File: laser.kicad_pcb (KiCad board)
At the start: 4 copper layers, 90.2 x 50.9 mm, 129 parts, among them IC201 ADM7172ACPZ-4.2-R7, IC202 LT1716CS5#TRPBF, IC203 ADM7154ARDZ-3.3-R7, IC204 IRF9358PBF, IC601 ATMEGA328P-AU, IC602 FT232RL-TUBE, IC701 MAX6126AASA25+, IC801 ADS122C04IPWR, J601 M20-9980345, J602 USB_Connector, Q401 RSR030N06TL, U101 281698-3, U201 LM4040EIM3X-2.5_NOPB, U301 OPA569AIDWPR, U302 OPA569AIDWPR, U401 ADA4528-2ACPZ-RL, U402 782853152_WE-CBA_08, U501 ADA4528-2ACPZ-RL, U502 ADA4528-2ACPZ-RL, U801 MAX5217GUA+, U802 MAX5217GUA+, Y601 ECS-160-16-33B-CKM-TR

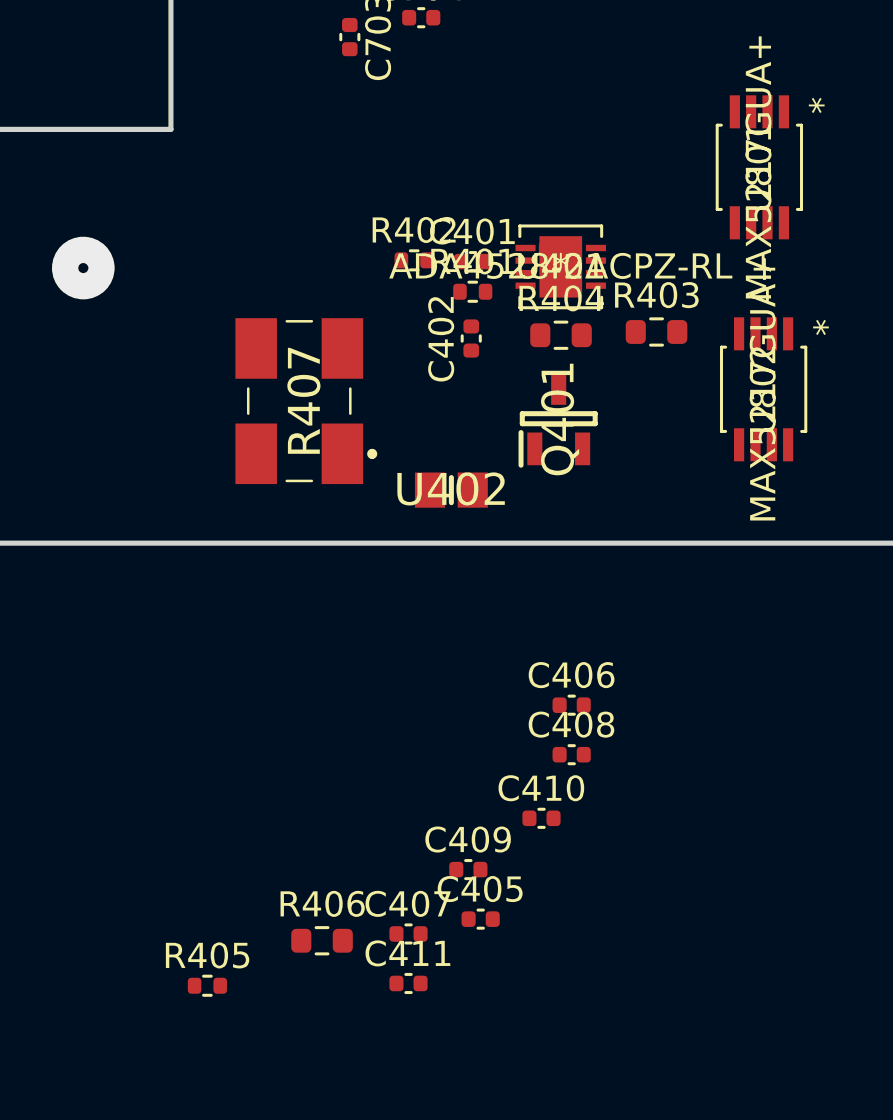
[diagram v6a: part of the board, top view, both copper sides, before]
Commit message: laid out reference and current resistors/caps
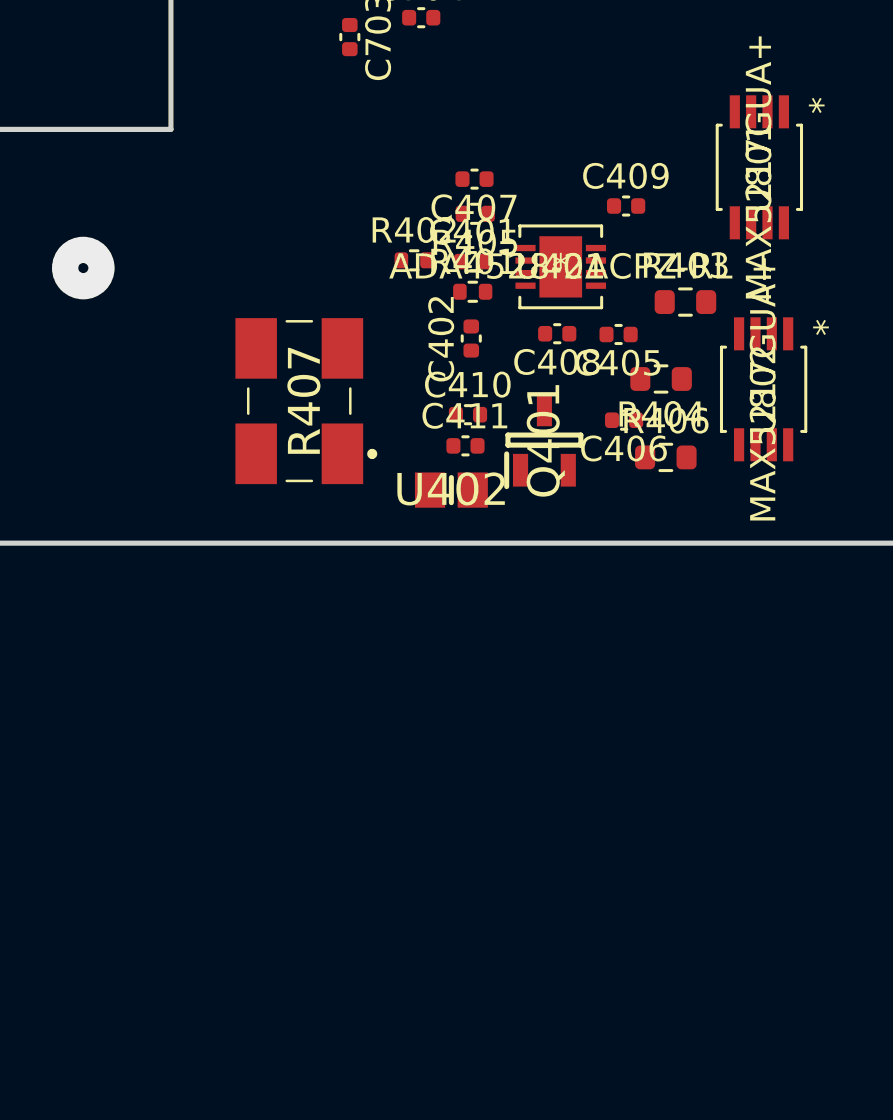
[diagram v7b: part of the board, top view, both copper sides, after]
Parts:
- moved R405 32.5 mm to (167.9, 119.1), turned to 180 degrees
- moved C407 30.1 mm to (167.9, 117.7), turned to 180 degrees
- moved C409 27.1 mm to (173.9, 118.8)
- moved C405 23.9 mm to (173.6, 123.9), turned to 180 degrees
- moved R406 23.6 mm to (175.5, 128.8)
- moved C411 21.5 mm to (167.5, 128.3)
- moved C408 16.8 mm to (171.2, 123.9), turned to 180 degrees
- moved C410 16.3 mm to (167.6, 127.1)
- moved C406 11.5 mm to (173.8, 127.3), turned to 180 degrees
- moved R404 4.34 mm to (175.3, 125.7), turned to 180 degrees
- moved R403 1.65 mm to (176.2, 122.6)
- moved Q401 1.02 mm to (170.6, 128.1)
- moved C403 0.13 mm to (171.3, 120.6)
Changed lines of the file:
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@@
   )
   (module Capacitor_SMD:C_0402_1005Metric (layer B.Cu)
-    (at 171.18 120.52)
+    (at 171.28 120.6)
     (descr "Capacitor SMD 0402 (1005 Metric), square (rectangular) end terminal, IPC_7351 nominal, (Body size source: IPC-SM-782 page 76, https://www.pcb-3d.com/wordpress/wp-content/uploads/ipc-sm-782a_amendment_1_and_2.pdf), generated with kicad-footprint-generator")
     (tags capacitor)
@@
   )
   (module Capacitor_SMD:C_0402_1005Metric (layer F.Cu)
-    (at 168.105001 147.165001)
+    (at 173.59 123.91 180)
     (descr "Capacitor SMD 0402 (1005 Metric), square (rectangular) end terminal, IPC_7351 nominal, (Body size source: IPC-SM-782 page 76, https://www.pcb-3d.com/wordpress/wp-content/uploads/ipc-sm-782a_amendment_1_and_2.pdf), generated with kicad-footprint-generator")
     (tags capacitor)
@@
       (effects (font (size 0.25 0.25) (thickness 0.04)))
     )
-    (pad 2 smd roundrect (at 0.48 0) (size 0.56 0.62) (layers F.Cu F.Paste F.Mask) (roundrect_rratio 0.25)
-      (net 126 GND))
-    (pad 1 smd roundrect (at -0.48 0) (size 0.56 0.62) (layers F.Cu F.Paste F.Mask) (roundrect_rratio 0.25)
+    (pad 2 smd roundrect (at 0.48 0 180) (size 0.56 0.62) (layers F.Cu F.Paste F.Mask) (roundrect_rratio 0.25)
+      (net 126 GND))
+    (pad 1 smd roundrect (at -0.48 0 180) (size 0.56 0.62) (layers F.Cu F.Paste F.Mask) (roundrect_rratio 0.25)
       (net 25 "Net-(C405-Pad1)"))
     (model ${KISYS3DMOD}/Capacitor_SMD.3dshapes/C_0402_1005Metric.wrl
@@
   )
   (module Capacitor_SMD:C_0402_1005Metric (layer F.Cu)
-    (at 171.725001 138.655001)
+    (at 173.81 127.32 180)
     (descr "Capacitor SMD 0402 (1005 Metric), square (rectangular) end terminal, IPC_7351 nominal, (Body size source: IPC-SM-782 page 76, https://www.pcb-3d.com/wordpress/wp-content/uploads/ipc-sm-782a_amendment_1_and_2.pdf), generated with kicad-footprint-generator")
     (tags capacitor)
@@
       (effects (font (size 0.25 0.25) (thickness 0.04)))
     )
-    (pad 1 smd roundrect (at -0.48 0) (size 0.56 0.62) (layers F.Cu F.Paste F.Mask) (roundrect_rratio 0.25)
+    (pad 1 smd roundrect (at -0.48 0 180) (size 0.56 0.62) (layers F.Cu F.Paste F.Mask) (roundrect_rratio 0.25)
       (net 26 "Net-(C406-Pad1)"))
-    (pad 2 smd roundrect (at 0.48 0) (size 0.56 0.62) (layers F.Cu F.Paste F.Mask) (roundrect_rratio 0.25)
-      (net 126 GND))
-    (model ${KISYS3DMOD}/Capacitor_SMD.3dshapes/C_0402_1005Metric.wrl
-      (at (xyz 0 0 0))
-      (scale (xyz 1 1 1))
-      (rotate (xyz 0 0 0))
-    )
-  )
-  (module Capacitor_SMD:C_0402_1005Metric (layer F.Cu)
-    (at 165.235001 147.755001)
+    (pad 2 smd roundrect (at 0.48 0 180) (size 0.56 0.62) (layers F.Cu F.Paste F.Mask) (roundrect_rratio 0.25)
+      (net 126 GND))
+    (model ${KISYS3DMOD}/Capacitor_SMD.3dshapes/C_0402_1005Metric.wrl
+      (at (xyz 0 0 0))
+      (scale (xyz 1 1 1))
+      (rotate (xyz 0 0 0))
+    )
+  )
+  (module Capacitor_SMD:C_0402_1005Metric (layer F.Cu)
+    (at 167.86 117.73 180)
     (descr "Capacitor SMD 0402 (1005 Metric), square (rectangular) end terminal, IPC_7351 nominal, (Body size source: IPC-SM-782 page 76, https://www.pcb-3d.com/wordpress/wp-content/uploads/ipc-sm-782a_amendment_1_and_2.pdf), generated with kicad-footprint-generator")
     (tags capacitor)
@@
       (effects (font (size 0.25 0.25) (thickness 0.04)))
     )
-    (pad 2 smd roundrect (at 0.48 0) (size 0.56 0.62) (layers F.Cu F.Paste F.Mask) (roundrect_rratio 0.25)
+    (pad 2 smd roundrect (at 0.48 0 180) (size 0.56 0.62) (layers F.Cu F.Paste F.Mask) (roundrect_rratio 0.25)
       (net 27 "Net-(C407-Pad2)"))
-    (pad 1 smd roundrect (at -0.48 0) (size 0.56 0.62) (layers F.Cu F.Paste F.Mask) (roundrect_rratio 0.25)
-      (net 126 GND))
-    (model ${KISYS3DMOD}/Capacitor_SMD.3dshapes/C_0402_1005Metric.wrl
-      (at (xyz 0 0 0))
-      (scale (xyz 1 1 1))
-      (rotate (xyz 0 0 0))
-    )
-  )
-  (module Capacitor_SMD:C_0402_1005Metric (layer F.Cu)
-    (at 171.725001 140.625001)
+    (pad 1 smd roundrect (at -0.48 0 180) (size 0.56 0.62) (layers F.Cu F.Paste F.Mask) (roundrect_rratio 0.25)
+      (net 126 GND))
+    (model ${KISYS3DMOD}/Capacitor_SMD.3dshapes/C_0402_1005Metric.wrl
+      (at (xyz 0 0 0))
+      (scale (xyz 1 1 1))
+      (rotate (xyz 0 0 0))
+    )
+  )
+  (module Capacitor_SMD:C_0402_1005Metric (layer F.Cu)
+    (at 171.15 123.88 180)
     (descr "Capacitor SMD 0402 (1005 Metric), square (rectangular) end terminal, IPC_7351 nominal, (Body size source: IPC-SM-782 page 76, https://www.pcb-3d.com/wordpress/wp-content/uploads/ipc-sm-782a_amendment_1_and_2.pdf), generated with kicad-footprint-generator")
     (tags capacitor)
@@
       (effects (font (size 0.25 0.25) (thickness 0.04)))
     )
-    (pad 1 smd roundrect (at -0.48 0) (size 0.56 0.62) (layers F.Cu F.Paste F.Mask) (roundrect_rratio 0.25)
+    (pad 1 smd roundrect (at -0.48 0 180) (size 0.56 0.62) (layers F.Cu F.Paste F.Mask) (roundrect_rratio 0.25)
       (net 28 "Net-(C408-Pad1)"))
-    (pad 2 smd roundrect (at 0.48 0) (size 0.56 0.62) (layers F.Cu F.Paste F.Mask) (roundrect_rratio 0.25)
-      (net 126 GND))
-    (model ${KISYS3DMOD}/Capacitor_SMD.3dshapes/C_0402_1005Metric.wrl
-      (at (xyz 0 0 0))
-      (scale (xyz 1 1 1))
-      (rotate (xyz 0 0 0))
-    )
-  )
-  (module Capacitor_SMD:C_0402_1005Metric (layer F.Cu)
-    (at 167.615001 145.195001)
+    (pad 2 smd roundrect (at 0.48 0 180) (size 0.56 0.62) (layers F.Cu F.Paste F.Mask) (roundrect_rratio 0.25)
+      (net 126 GND))
+    (model ${KISYS3DMOD}/Capacitor_SMD.3dshapes/C_0402_1005Metric.wrl
+      (at (xyz 0 0 0))
+      (scale (xyz 1 1 1))
+      (rotate (xyz 0 0 0))
+    )
+  )
+  (module Capacitor_SMD:C_0402_1005Metric (layer F.Cu)
+    (at 173.89 118.8)
     (descr "Capacitor SMD 0402 (1005 Metric), square (rectangular) end terminal, IPC_7351 nominal, (Body size source: IPC-SM-782 page 76, https://www.pcb-3d.com/wordpress/wp-content/uploads/ipc-sm-782a_amendment_1_and_2.pdf), generated with kicad-footprint-generator")
     (tags capacitor)
@@
   )
   (module Capacitor_SMD:C_0402_1005Metric (layer F.Cu)
-    (at 170.525001 143.155001)
+    (at 167.6 127.1)
     (descr "Capacitor SMD 0402 (1005 Metric), square (rectangular) end terminal, IPC_7351 nominal, (Body size source: IPC-SM-782 page 76, https://www.pcb-3d.com/wordpress/wp-content/uploads/ipc-sm-782a_amendment_1_and_2.pdf), generated with kicad-footprint-generator")
     (tags capacitor)
@@
   )
   (module Capacitor_SMD:C_0402_1005Metric (layer F.Cu)
-    (at 165.235001 149.725001)
+    (at 167.5 128.34)
     (descr "Capacitor SMD 0402 (1005 Metric), square (rectangular) end terminal, IPC_7351 nominal, (Body size source: IPC-SM-782 page 76, https://www.pcb-3d.com/wordpress/wp-content/uploads/ipc-sm-782a_amendment_1_and_2.pdf), generated with kicad-footprint-generator")
     (tags capacitor)
@@
   )
   (module "footprint libraries:RSR030N06TL" (layer F.Cu)
-    (at 171.21 127.26 90)
+    (at 170.64 128.11 90)
     (descr SOT-346)
     (tags Transistor)
@@
   )
   (module Resistor_SMD:R_0603_1608Metric (layer F.Cu)
-    (at 175.1 123.81)
+    (at 176.25 122.62)
     (descr "Resistor SMD 0603 (1608 Metric), square (rectangular) end terminal, IPC_7351 nominal, (Body size source: IPC-SM-782 page 72, https://www.pcb-3d.com/wordpress/wp-content/uploads/ipc-sm-782a_amendment_1_and_2.pdf), generated with kicad-footprint-generator")
     (tags resistor)
@@
   )
   (module Resistor_SMD:R_0603_1608Metric (layer F.Cu)
-    (at 171.3 123.94)
+    (at 175.28 125.68 180)
     (descr "Resistor SMD 0603 (1608 Metric), square (rectangular) end terminal, IPC_7351 nominal, (Body size source: IPC-SM-782 page 72, https://www.pcb-3d.com/wordpress/wp-content/uploads/ipc-sm-782a_amendment_1_and_2.pdf), generated with kicad-footprint-generator")
     (tags resistor)
@@
       (effects (font (size 0.4 0.4) (thickness 0.06)))
     )
-    (pad 2 smd roundrect (at 0.825 0) (size 0.8 0.95) (layers F.Cu F.Paste F.Mask) (roundrect_rratio 0.25)
+    (pad 2 smd roundrect (at 0.825 0 180) (size 0.8 0.95) (layers F.Cu F.Paste F.Mask) (roundrect_rratio 0.25)
       (net 25 "Net-(C405-Pad1)"))
-    (pad 1 smd roundrect (at -0.825 0) (size 0.8 0.95) (layers F.Cu F.Paste F.Mask) (roundrect_rratio 0.25)
+    (pad 1 smd roundrect (at -0.825 0 180) (size 0.8 0.95) (layers F.Cu F.Paste F.Mask) (roundrect_rratio 0.25)
       (net 26 "Net-(C406-Pad1)"))
     (model ${KISYS3DMOD}/Resistor_SMD.3dshapes/R_0603_1608Metric.wrl
@@
   )
   (module Resistor_SMD:R_0402_1005Metric (layer F.Cu)
-    (at 157.235001 149.815001)
+    (at 167.89 119.11 180)
     (descr "Resistor SMD 0402 (1005 Metric), square (rectangular) end terminal, IPC_7351 nominal, (Body size source: IPC-SM-782 page 72, https://www.pcb-3d.com/wordpress/wp-content/uploads/ipc-sm-782a_amendment_1_and_2.pdf), generated with kicad-footprint-generator")
     (tags resistor)
@@
       (effects (font (size 0.26 0.26) (thickness 0.04)))
     )
-    (pad 1 smd roundrect (at -0.51 0) (size 0.54 0.64) (layers F.Cu F.Paste F.Mask) (roundrect_rratio 0.25)
+    (pad 1 smd roundrect (at -0.51 0 180) (size 0.54 0.64) (layers F.Cu F.Paste F.Mask) (roundrect_rratio 0.25)
       (net 100 "Net-(R402-Pad2)"))
-    (pad 2 smd roundrect (at 0.51 0) (size 0.54 0.64) (layers F.Cu F.Paste F.Mask) (roundrect_rratio 0.25)
+    (pad 2 smd roundrect (at 0.51 0 180) (size 0.54 0.64) (layers F.Cu F.Paste F.Mask) (roundrect_rratio 0.25)
       (net 27 "Net-(C407-Pad2)"))
     (model ${KISYS3DMOD}/Resistor_SMD.3dshapes/R_0402_1005Metric.wrl
@@
   )
   (module Resistor_SMD:R_0603_1608Metric (layer F.Cu)
-    (at 161.795001 148.025001)
+    (at 175.47 128.8)
     (descr "Resistor SMD 0603 (1608 Metric), square (rectangular) end terminal, IPC_7351 nominal, (Body size source: IPC-SM-782 page 72, https://www.pcb-3d.com/wordpress/wp-content/uploads/ipc-sm-782a_amendment_1_and_2.pdf), generated with kicad-footprint-generator")
     (tags resistor)

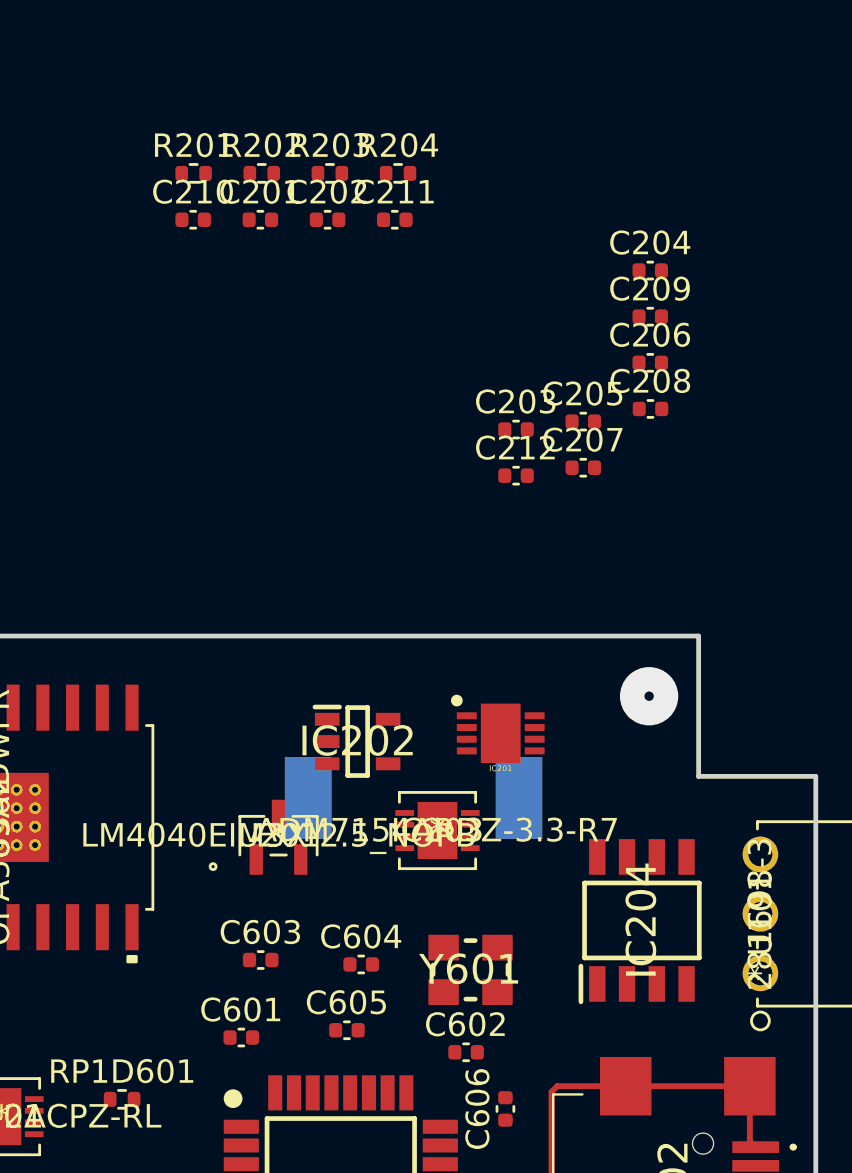
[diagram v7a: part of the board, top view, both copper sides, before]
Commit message: finish placing power supply
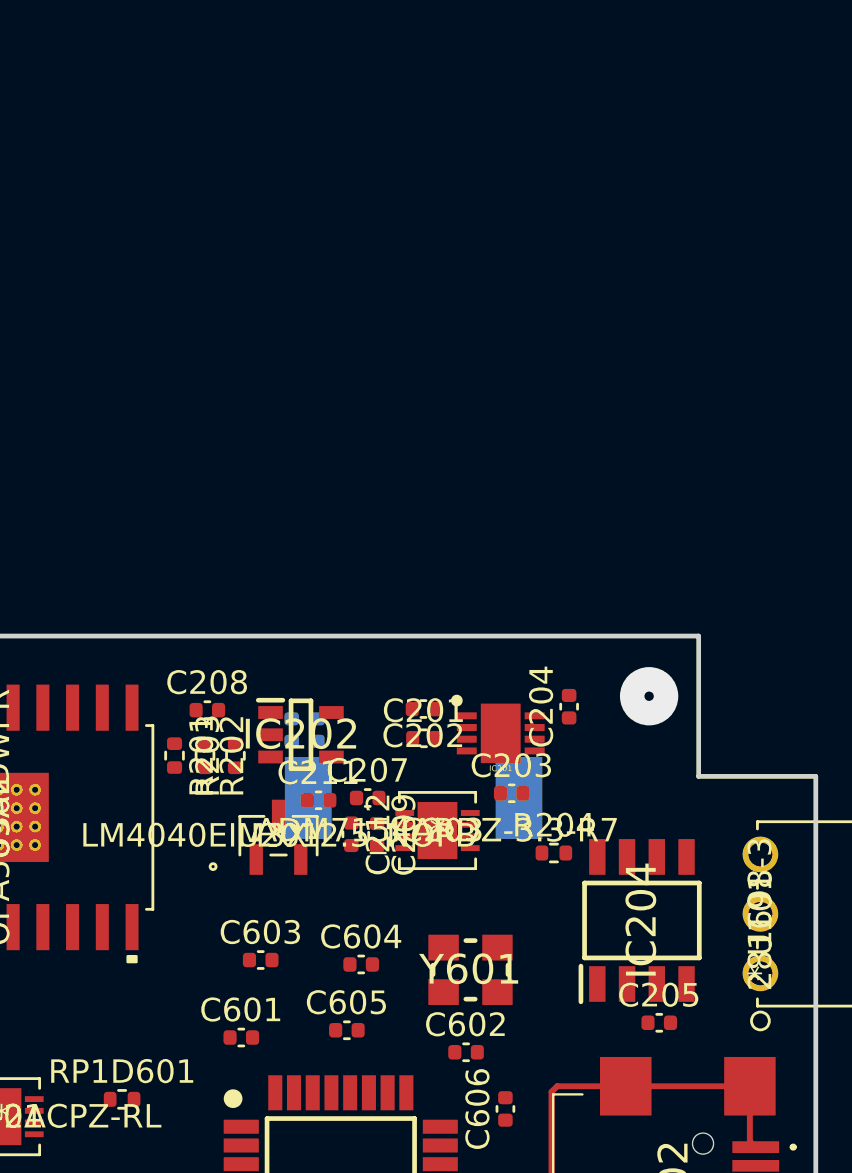
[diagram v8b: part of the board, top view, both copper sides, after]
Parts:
- C206, C210: moved to B.Cu
- moved R204 29.8 mm to (201.8, 90.6)
- moved C205 25.9 mm to (206.3, 97.8)
- moved R203 25.2 mm to (188.2, 86.5), turned to 90 degrees
- moved C209 25.0 mm to (194.2, 89.8), turned to 270 degrees
- moved C211 25.0 mm to (191.8, 88.3)
- moved R202 25.0 mm to (186.9, 86.5), turned to 270 degrees
- moved R201 24.9 mm to (185.6, 86.4), turned to 270 degrees
- moved C201 23.2 mm to (196.2, 85.7)
- moved C208 22.9 mm to (187.0, 84.5)
- moved C210 22.4 mm to (191.7, 85.3), turned to 90 degrees
- moved C206 21.9 mm to (190.6, 85.3), turned to 90 degrees
- moved C202 21.3 mm to (196.2, 84.5), turned to 180 degrees
- moved C204 18.9 mm to (202.4, 84.3), turned to 90 degrees
- moved C212 16.9 mm to (193.2, 89.8), turned to 270 degrees
- moved C207 16.8 mm to (193.8, 88.2)
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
